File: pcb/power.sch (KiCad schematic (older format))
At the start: 19 parts

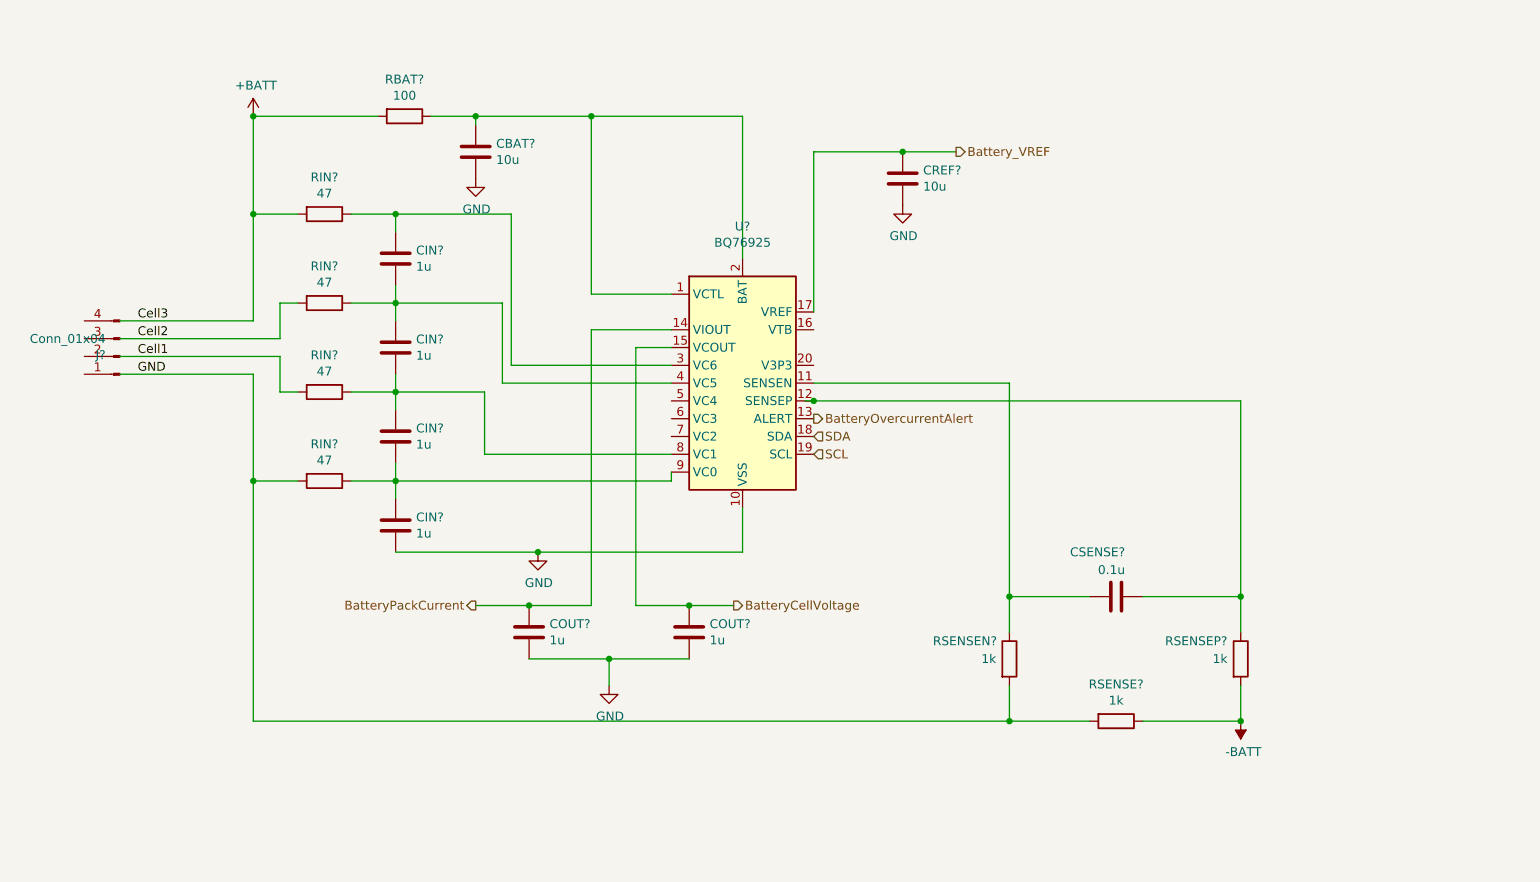
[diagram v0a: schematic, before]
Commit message: Cell voltage, BATT+, current sensor and VCTL changed. Changes to lib changed the other .sch
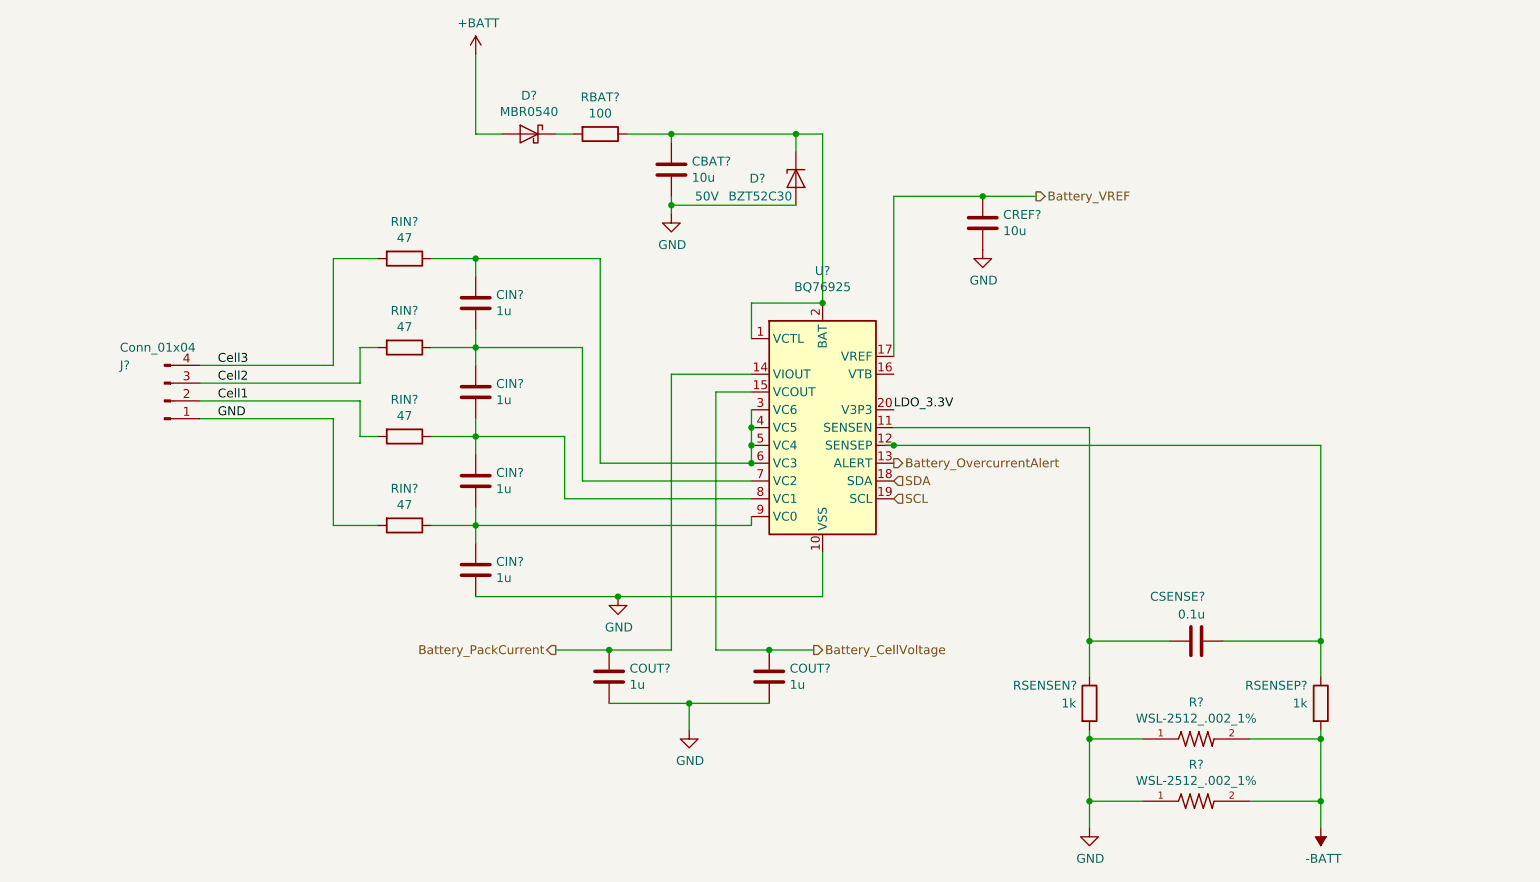
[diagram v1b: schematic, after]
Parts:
- removed RSENSE?: 1k, Resistor_SMD:R_0805_2012Metric, symbol Device:R
- added D?: BZT52C30, Diode_SMD:D_SOD-123, symbol Diode:BZT52Bxx
- added D?: MBR0540, Diode_SMD:D_SOD-123, symbol Diode:MBR0540
- added R? (x2): WSL-2512_.002_1%, RESC1005X40, symbol rasbot:WSL-2512_.002_1%
- CBAT?: Voltage (none) -> 50V
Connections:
- net labels added: Battery_CellVoltage, Battery_OvercurrentAlert, Battery_PackCurrent, LDO_3.3V
- net labels removed: BatteryCellVoltage, BatteryOvercurrentAlert, BatteryPackCurrent
- wire segments 75 -> 87
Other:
- moved on the sheet: CBAT?, CIN?, COUT?, CREF?, CSENSE?, J?, RBAT?, RIN?, RSENSEN?, RSENSEP?, U?

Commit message: Thermistor added
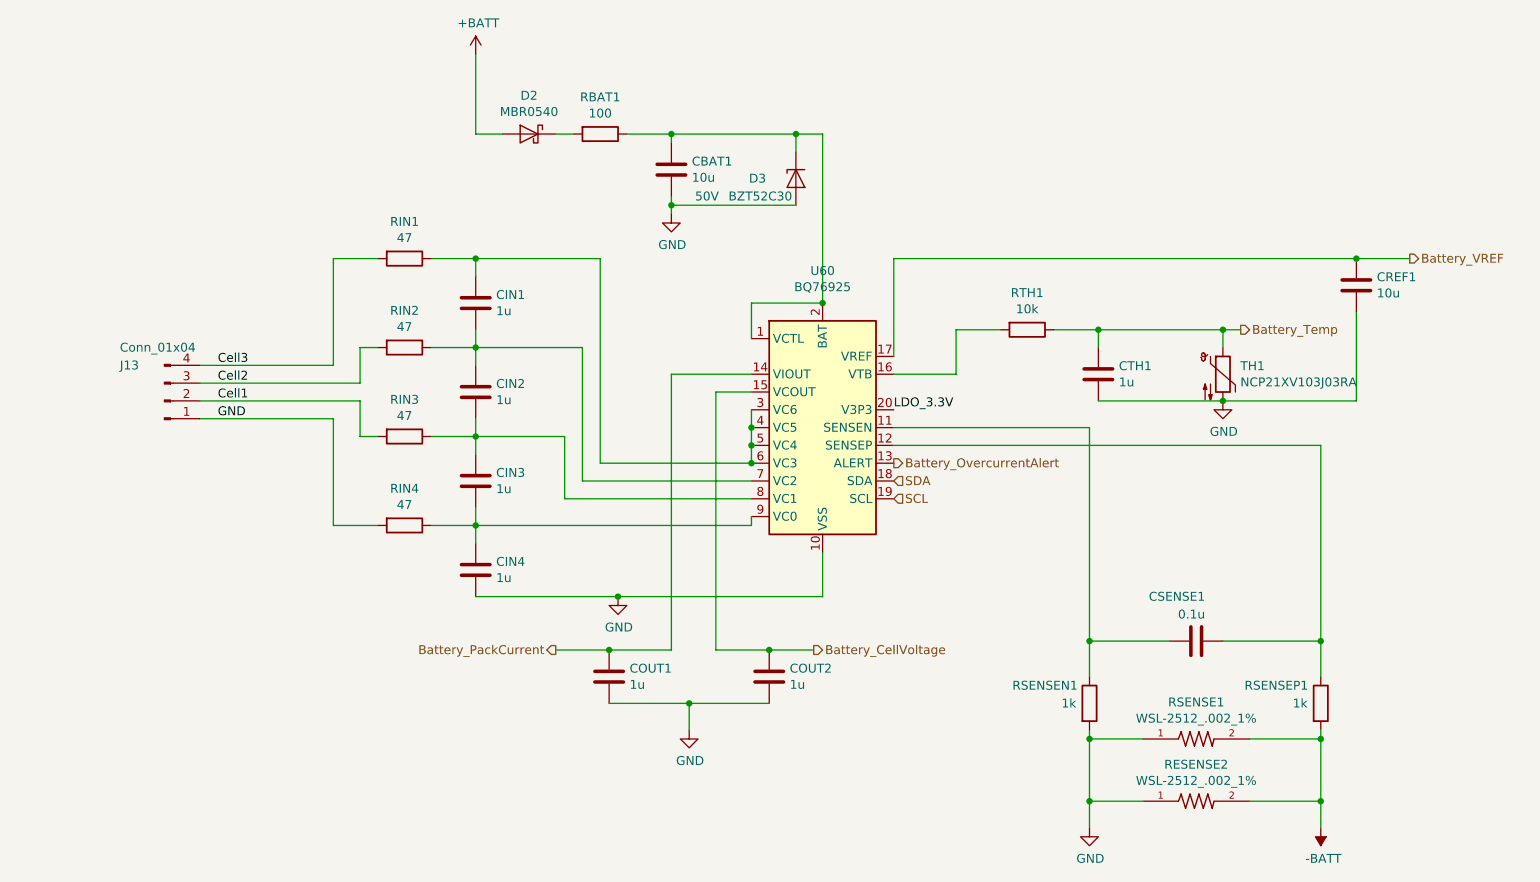
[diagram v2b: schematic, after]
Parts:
- added CTH1: 1u, Capacitor_SMD:C_0805_2012Metric, symbol Device:C
- added RTH1: 10k, Resistor_SMD:R_0805_2012Metric, symbol Device:R
- added TH1: NCP21XV103J03RA, Resistor_SMD:R_0805_2012Metric, symbol Device:Thermistor_NTC
- gave numbers to parts that had none: 22
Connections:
- net GND: now also CTH1.2, TH1.2
- net at U60.16 (VTB): now also RTH1.2
- new net Battery_Temp: CTH1.1, RTH1.1, TH1.1
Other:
- moved on the sheet: CREF1
